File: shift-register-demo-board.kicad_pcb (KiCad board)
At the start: 2 copper layers, 95 parts, among them J1 Conn_01x12_Pin, J2 Conn_01x12_Pin, SW1 SW_Push, SW2 SW_Push, SW3 SW_Push, SW4 SW_Push, U1 M24C64-RMN6TP, U2 W25Q128JVS, U3 74HC595, U4 SN65HVD230, U5 PCF8563T, U6 74HC595, U7 74HC14, U8 74HC165, Y1 32k768Hz

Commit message: Rough component placement started.  WIP
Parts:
- moved C5 79.8 mm to (125.7, 52.8), turned to 180 degrees
- moved U5 76.9 mm to (124.0, 56.4)
- moved R18 70.6 mm to (128.5, 54.9), turned to -90 degrees
- moved C8 69.1 mm to (115.3, 52.3), turned to 180 degrees
- moved C9 68.2 mm to (115.3, 58.4), turned to 180 degrees
- moved C3 65.9 mm to (93.5, 86.4), turned to 180 degrees
- moved R3 63.1 mm to (96.0, 88.9), turned to -90 degrees
- moved R19 61.6 mm to (119.4, 58.4), turned to 90 degrees
- moved C7 58.1 mm to (100.3, 71.6), turned to 180 degrees
- moved R4 56.0 mm to (84.8, 91.9), turned to 90 degrees
- moved R26 55.0 mm to (106.7, 82.8)
- moved R5 53.1 mm to (83.3, 91.9), turned to 90 degrees
- moved C2 50.9 mm to (92.8, 58.4), turned to 90 degrees
- moved R1 45.9 mm to (96.0, 43.7), turned to 180 degrees
- moved R2 42.7 mm to (93.0, 43.7), turned to 180 degrees
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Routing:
- net GND: track 0.00 -> 48.7 mm, vias 0 -> 31
- net +3V3: track 0.00 -> 26.3 mm, vias 0 -> 6
- net /OSC_OUT: track 0.00 -> 8.99 mm
- net /OSC_IN: track 0.00 -> 8.49 mm
- net /EEPROM_E0: track 0.00 -> 7.53 mm
- net /EEPROM_E1: track 0.00 -> 6.11 mm
- net FLASH_nCS: track 0.00 -> 5.61 mm
- net /EEPROM_E2: track 0.00 -> 4.13 mm
- net /LED8_K: track 0.00 -> 4.09 mm
- net /LED7_K: track 0.00 -> 3.65 mm
- net /LED6_K: track 0.00 -> 3.35 mm
- net /LED5_K: track 0.00 -> 2.63 mm
- net /RTC_nINT: track 0.00 -> 2.33 mm
- net CANH: track 0.00 -> 2.29 mm
- net /LED4_K: track 0.00 -> 2.24 mm
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
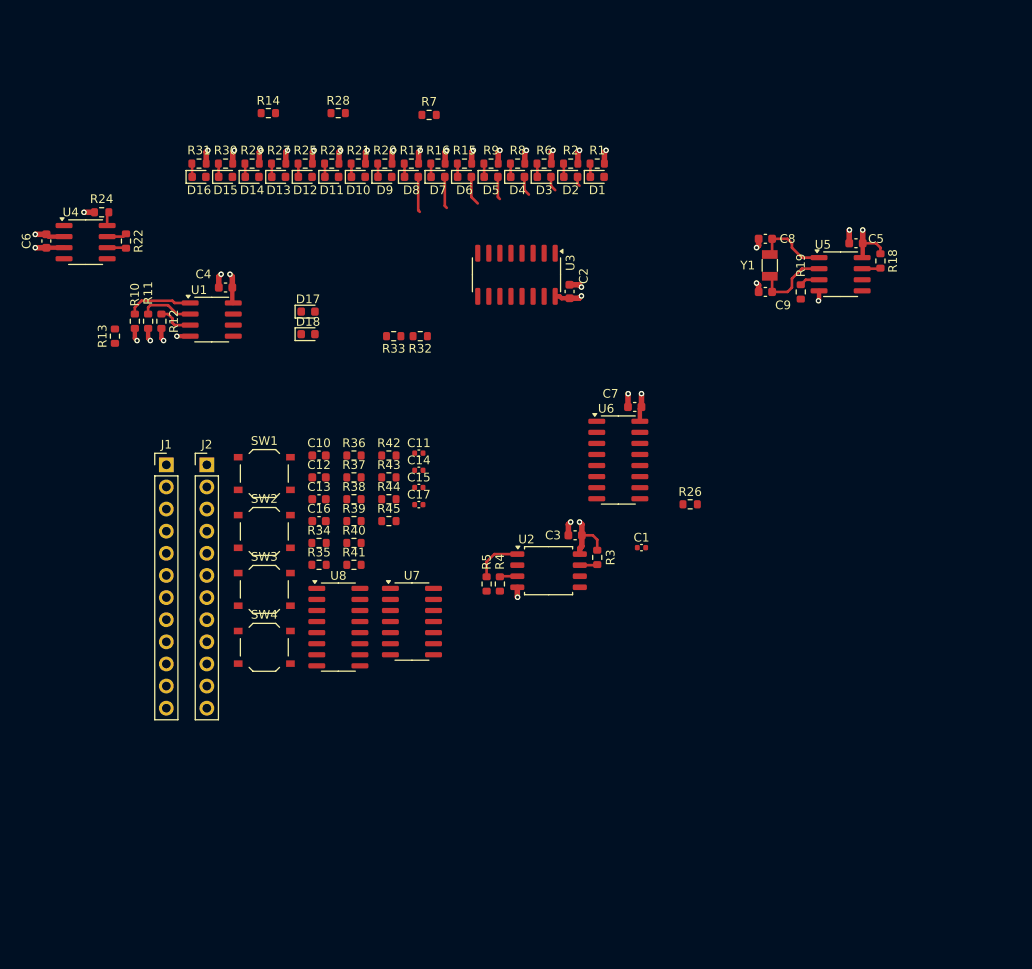
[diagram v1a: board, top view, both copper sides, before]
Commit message: Added 2 more pushbuttons to the 74HC165 through the Schmitt trigger inverter, removed provision for unused 74HC14 inverters as a result
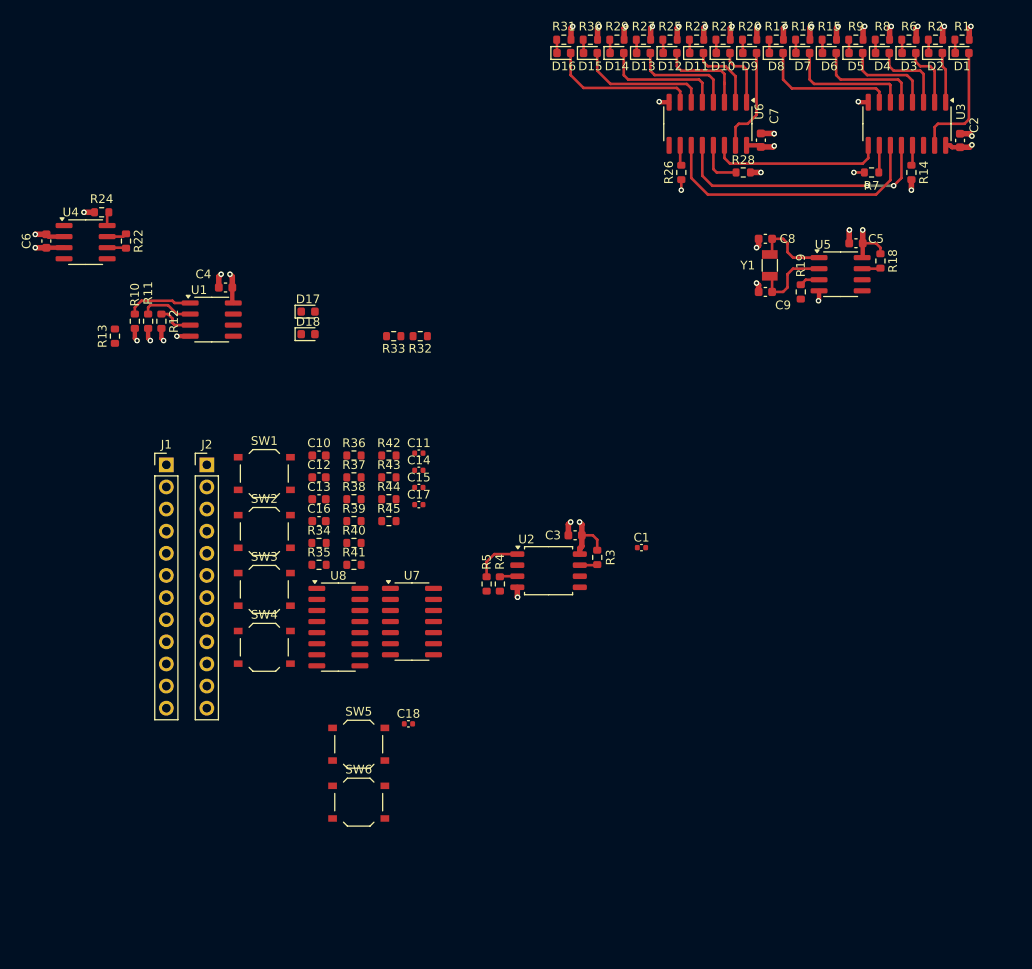
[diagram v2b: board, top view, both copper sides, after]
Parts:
- added C18: 100nF, Capacitor_SMD:C_0402_1005Metric, F.Cu at (74.3, 108.0)
- added SW5: SW_Push, Button_Switch_SMD:SW_Push_1P1T_XKB_TS-1187A, F.Cu at (68.6, 110.3)
- added SW6: SW_Push, Button_Switch_SMD:SW_Push_1P1T_XKB_TS-1187A, F.Cu at (68.6, 117.0)
- moved R14 74.1 mm to (132.1, 44.7), turned to -90 degrees
- moved R7 51.2 mm to (127.5, 44.7), turned to 0 degrees
- moved C2 48.1 mm to (137.7, 41.0)
- moved U3 48.1 mm to (131.6, 39.1)
- moved R28 47.0 mm to (112.8, 44.7)
- moved D1 44.2 mm to (137.9, 31.0)
- moved D10 44.2 mm to (110.5, 31.0)
- moved D11 44.2 mm to (107.4, 31.0)
- moved D15 44.2 mm to (95.2, 31.0)
- moved D16 44.2 mm to (92.2, 31.0)
- moved D2 44.2 mm to (134.8, 31.0)
- moved D3 44.2 mm to (131.8, 31.0)
- moved D4 44.2 mm to (128.8, 31.0)
- moved D5 44.2 mm to (125.7, 31.0)
- moved D7 44.2 mm to (119.6, 31.0)
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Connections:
- net /Connectors-Pushbuttons/INV_GPIO_A renamed SW5
- net /Connectors-Pushbuttons/INV_GPIO_B renamed SW6
- net /LED_OE renamed /SIPO1_OE
- net /ROW_CLR renamed /SIPO1_CLR
- C1 pad 1: unconnected-(C1-Pad1) -> /Connectors-Pushbuttons/SW5_PU
- C1 pad 2: unconnected-(C1-Pad2) -> GND
- R37 pad 1: /Connectors-Pushbuttons/D2 -> /Connectors-Pushbuttons/D4
- R38 pad 1: /Connectors-Pushbuttons/D3 -> /Connectors-Pushbuttons/D5
- R39 pad 1: /Connectors-Pushbuttons/D4 -> /Connectors-Pushbuttons/D6
- R40 pad 1: /Connectors-Pushbuttons/D5 -> /Connectors-Pushbuttons/D7
- R41 pad 1: /Connectors-Pushbuttons/D6 -> +3V3
- R41 pad 2: GND -> /Connectors-Pushbuttons/SW5_PU
- R42 pad 1: /Connectors-Pushbuttons/D7 -> +3V3
- R42 pad 2: GND -> /Connectors-Pushbuttons/SW5_PU
- U7 pad 11: /Connectors-Pushbuttons/GPIO_A -> /Connectors-Pushbuttons/SW5_PU
- U7 pad 13: /Connectors-Pushbuttons/GPIO_B -> /Connectors-Pushbuttons/SW5_PU
- U7 pad 6: SW3 -> /Connectors-Pushbuttons/SW3
- U7 pad 8: SW4 -> /Connectors-Pushbuttons/SW4
- U8 pad 13: /Connectors-Pushbuttons/D2 -> /Connectors-Pushbuttons/SW3
- U8 pad 14: /Connectors-Pushbuttons/D3 -> /Connectors-Pushbuttons/SW4
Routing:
- net LED_CLK: track 0.00 -> 32.1 mm
- net LED_LATCH: track 0.00 -> 30.9 mm, vias 0 -> 2
- net /SIPO2_DATA: track 0.00 -> 20.0 mm
- net /LED16_K: track 0.00 -> 17.1 mm
- net /LED15_K: track 0.00 -> 15.3 mm
- net /LED14_K: track 0.00 -> 14.1 mm
- net /LED1_K: track 0.00 -> 14.0 mm
- net /LED13_K: track 0.00 -> 12.3 mm
- net /LED9_K: track 0.00 -> 12.2 mm
- net /LED8_K: track 4.09 -> 15.9 mm
- net /LED12_K: track 0.00 -> 11.7 mm
- net /LED7_K: track 3.65 -> 14.6 mm
- net /LED6_K: track 3.35 -> 12.6 mm
- net /LED11_K: track 0.00 -> 8.37 mm
- net /LED5_K: track 2.63 -> 10.7 mm
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
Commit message: Changed 100nF caps from 0402 to 0603 footprints.  Grouped all pushbuttons together and routed to PISO shift reg
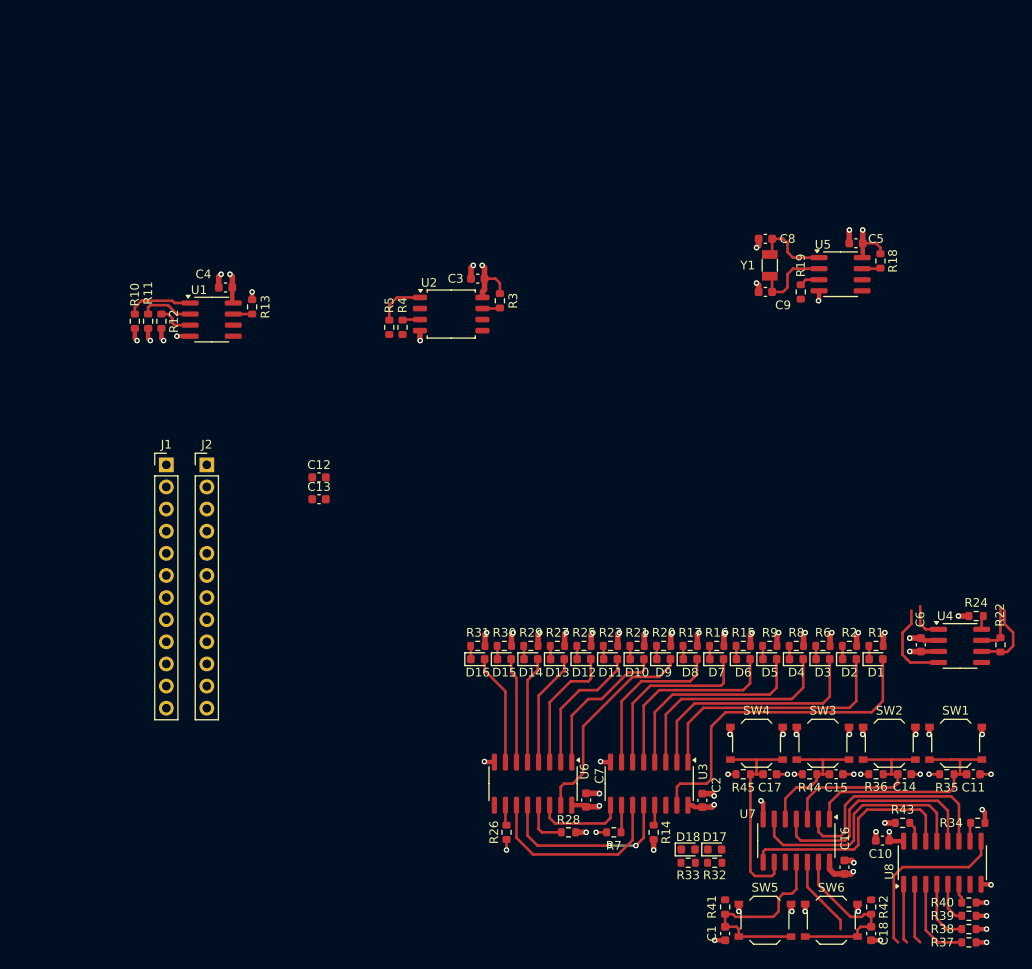
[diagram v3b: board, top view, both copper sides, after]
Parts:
- C1, C11, C14, C15, C17, C18: footprint Capacitor_SMD:C_0402_1005Metric -> Capacitor_SMD:C_0603_1608Metric
- moved C6 110.6 mm to (133.2, 98.9)
- moved R22 110.6 mm to (142.3, 98.9)
- moved U4 110.6 mm to (137.7, 99.1)
- moved R24 110.6 mm to (139.5, 95.6)
- moved R37 88.5 mm to (138.7, 133.1)
- moved R38 86.1 mm to (138.7, 131.6)
- moved SW1 85.2 mm to (137.2, 110.2)
- moved R39 83.9 mm to (138.7, 130.0)
- moved R34 82.2 mm to (139.7, 119.4)
- moved R40 81.8 mm to (138.7, 128.5)
- moved C2 81.3 mm to (108.1, 116.8)
- moved R14 81.3 mm to (102.5, 120.5)
- moved R7 81.3 mm to (97.9, 120.5)
- moved U3 81.3 mm to (102.0, 114.9)
- moved C7 78.4 mm to (94.7, 116.8)
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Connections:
- net Net-(U8-~{CE}) renamed /Connectors-Pushbuttons/BUTTON_CE
- C18 pad 1: /Connectors-Pushbuttons/SW5_PU -> /Connectors-Pushbuttons/SW6_PU
- R42 pad 2: /Connectors-Pushbuttons/SW5_PU -> /Connectors-Pushbuttons/SW6_PU
- SW6 pad 2: /Connectors-Pushbuttons/SW5_PU -> /Connectors-Pushbuttons/SW6_PU
- U7 pad 13: /Connectors-Pushbuttons/SW5_PU -> /Connectors-Pushbuttons/SW6_PU
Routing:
- net GND: track 53.4 -> 85.2 mm, vias 35 -> 64
- net /Connectors-Pushbuttons/SW3: track 0.00 -> 28.3 mm
- net /Connectors-Pushbuttons/SW1_PU: track 0.00 -> 27.5 mm
- net /Connectors-Pushbuttons/SW2: track 0.00 -> 27.2 mm
- net /Connectors-Pushbuttons/SW4: track 0.00 -> 26.9 mm
- net /Connectors-Pushbuttons/SW1: track 0.00 -> 26.1 mm
- net /Connectors-Pushbuttons/SW4_PU: track 0.00 -> 24.7 mm
- net /LED1_K: track 14.0 -> 38.2 mm
- net /Connectors-Pushbuttons/SW2_PU: track 0.00 -> 23.9 mm
- net /LED2_K: track 5.81 -> 29.6 mm
- net /Connectors-Pushbuttons/SW5_PU: track 0.00 -> 23.6 mm
- net /LED3_K: track 7.22 -> 27.7 mm
- net BUTTON_DATA: track 0.00 -> 20.4 mm
- net /Connectors-Pushbuttons/SW6_PU: track 0.00 -> 20.2 mm
- net /LED4_K: track 9.07 -> 25.8 mm
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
